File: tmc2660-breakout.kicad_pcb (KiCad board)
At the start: 2 copper layers, 26.9 x 31.1 mm, 21 parts, among them P1 SPI, P2 StepDir, P3 Motor, P4 VCC, P5 VMOT, U1 TMC2660

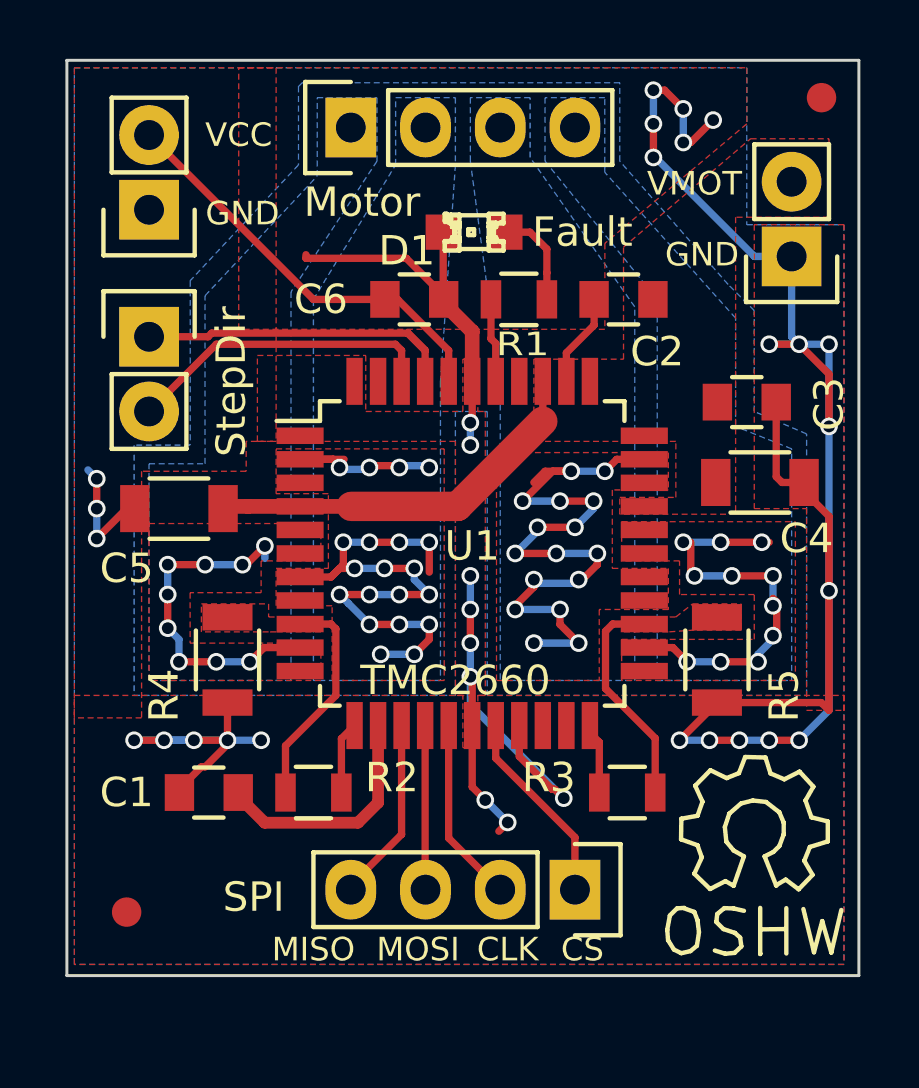
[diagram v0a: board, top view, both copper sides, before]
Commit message: o Add alternative footprint for shunt (2512 is more appropriate)
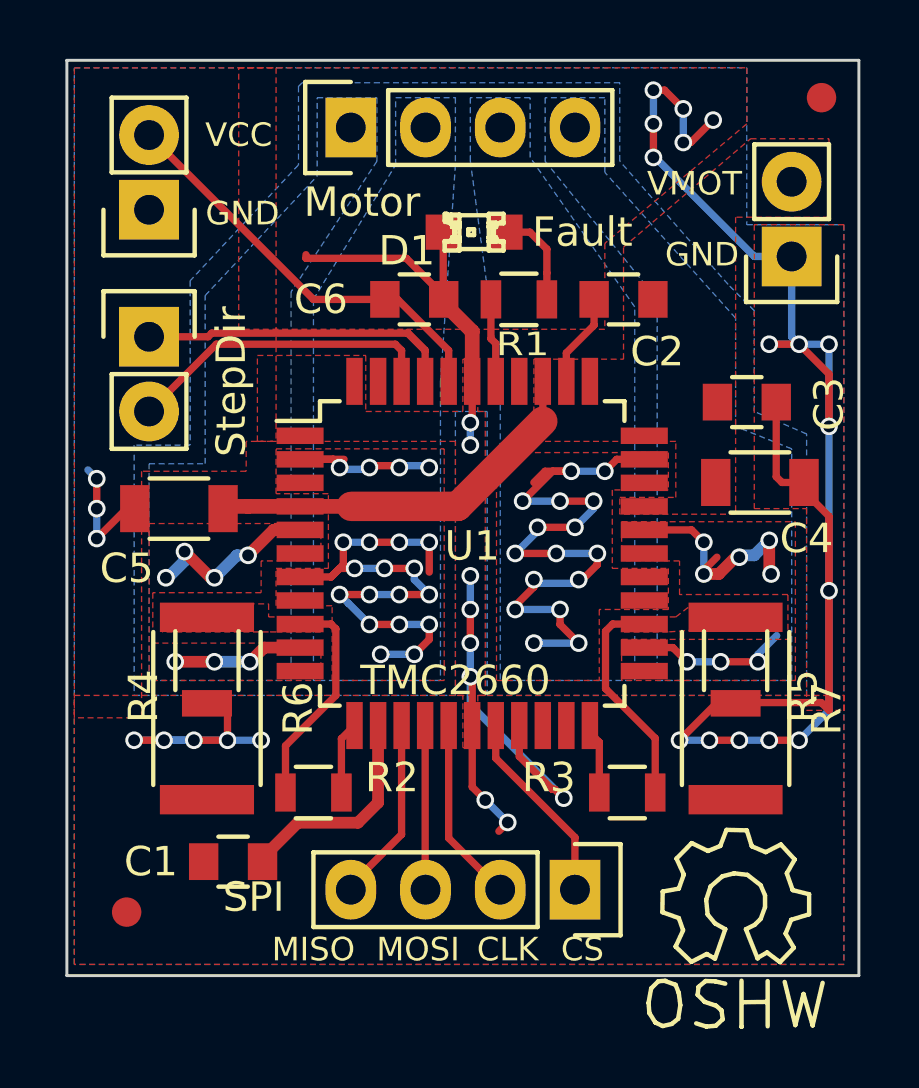
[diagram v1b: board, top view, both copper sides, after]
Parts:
- added R6: 0.075, Resistors_SMD:R_2512, F.Cu at (120.8, 59.6)
- added R7: 0.075, Resistors_SMD:R_2512, F.Cu at (138.8, 59.6)
- moved REF** 2.56 mm to (138.8, 66.2)
- moved C1 2.49 mm to (121.7, 64.8)
- moved R4 0.70 mm to (120.8, 58.0)
- moved R5 0.64 mm to (138.8, 58.0)
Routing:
- net GND: track 103.4 -> 101.0 mm
- net 1A2: track 11.9 -> 10.8 mm, vias 9 -> 7
- net Net-(C1-Pad1): track 8.15 -> 7.45 mm
- net 1B2: track 13.8 -> 13.2 mm, vias 11 -> 8

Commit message: o Widen the other 1206 pad to match the 2512 pad to avoid tombstoning
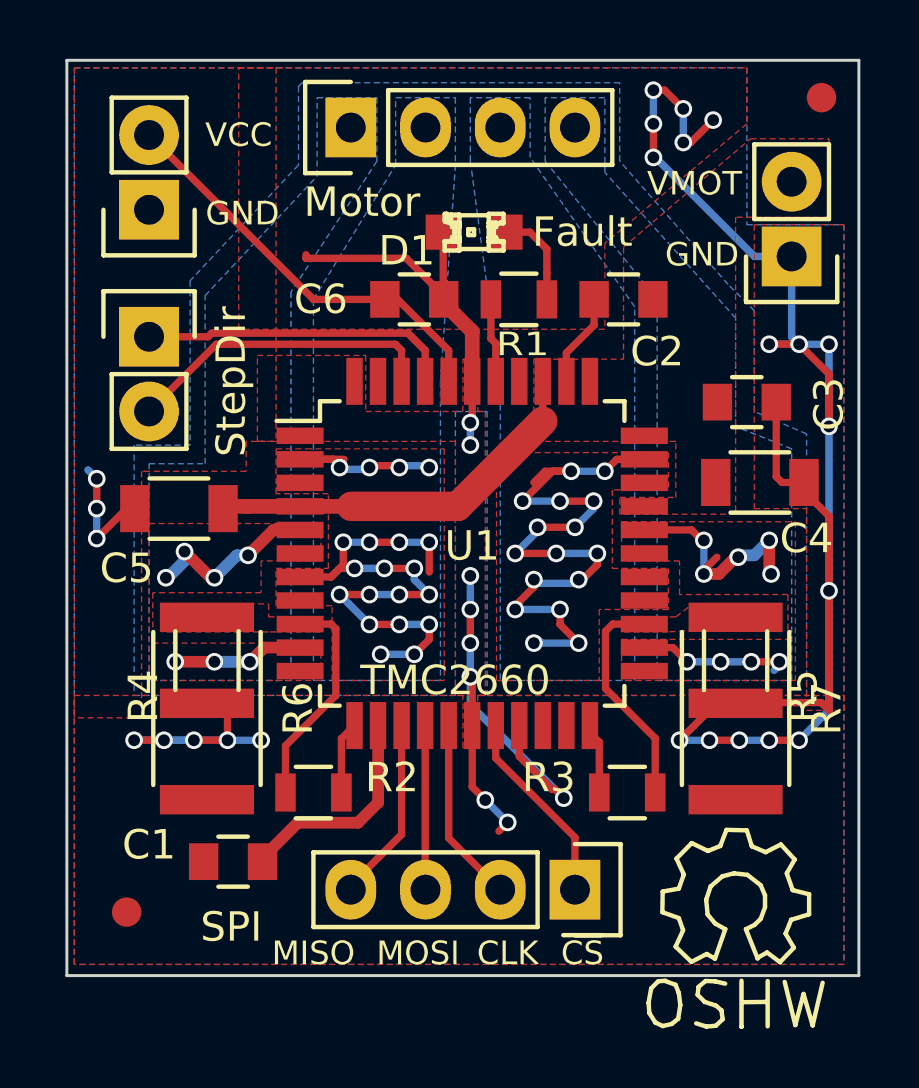
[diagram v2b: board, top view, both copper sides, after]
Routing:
- net 1B2: vias 8 -> 9
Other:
- board text added: "~CS"
- board text removed: "CS"
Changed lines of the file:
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@@
-(kicad_pcb (version 4) (host pcbnew "(2015-08-05 BZR 6054, Git 5c8efeb)-product")
+(kicad_pcb (version 4) (host pcbnew "(2016-01-05 BZR 6425, Git 89c183f)-product")
   (general
     (links 60)
@@
     (thickness 1.6)
     (drawings 13)
-    (tracks 312)
+    (tracks 314)
     (zones 0)
     (modules 23)
@@
   (layers
     (0 F.Cu signal)
-    (31 B.Cu signal hide)
+    (31 B.Cu signal)
     (32 B.Adhes user)
     (33 F.Adhes user)
@@
   )
   (setup
-    (last_trace_width 0.4)
+    (last_trace_width 0.25)
     (user_trace_width 0.4)
     (trace_clearance 0.127)
@@
     (mod_text_size 1 1)
     (mod_text_width 0.15)
-    (pad_size 1.5 1.5)
-    (pad_drill 0.6)
+    (pad_size 1 3.2)
+    (pad_drill 0)
     (pad_to_mask_clearance 0)
     (aux_axis_origin 0 0)
@@
     (pad 1 smd rect (at -1.45 0 270) (size 0.9 1.7) (layers F.Cu F.Paste F.Mask)
       (net 5 "Net-(R3-Pad1)"))
-    (pad 2 smd rect (at 1.45 0 270) (size 0.9 1.7) (layers F.Cu F.Paste F.Mask)
+    (pad 2 smd rect (at 1.45 0 270) (size 1 3.2) (layers F.Cu F.Paste F.Mask)
       (net 7 GND))
   )
@@
     (tags "capacitor 0805")
     (attr smd)
-    (fp_text reference C1 (at 2.794 0 180) (layer F.SilkS)
-      (effects (font (size 1 1) (thickness 0.15)))
-    )
-    (fp_text value 470n (at 1.016 -1.778 180) (layer F.Fab)
+    (fp_text reference C1 (at 2.8575 0.5715 180) (layer F.SilkS)
+      (effects (font (size 1 1) (thickness 0.15)))
+    )
+    (fp_text value 470n (at 3.8735 1.0795 180) (layer F.Fab)
       (effects (font (size 1 1) (thickness 0.15)))
     )
@@
       (effects (font (size 1 1) (thickness 0.15)))
     )
-    (fp_text value SPI (at 0.254 10.922 360) (layer F.SilkS)
+    (fp_text value SPI (at 1.27 11.684 360) (layer F.SilkS)
       (effects (font (size 1 1) (thickness 0.15)))
     )
@@
     (pad 1 smd rect (at -1.45 0 270) (size 0.9 1.7) (layers F.Cu F.Paste F.Mask)
       (net 3 "Net-(R2-Pad1)"))
-    (pad 2 smd rect (at 1.45 0 270) (size 0.9 1.7) (layers F.Cu F.Paste F.Mask)
+    (pad 2 smd rect (at 1.45 0 270) (size 1 3.2) (layers F.Cu F.Paste F.Mask)
       (net 7 GND))
   )
@@
     (effects (font (size 0.8 0.8) (thickness 0.15)))
   )
-  (gr_text "MOSI\n" (at 128.016 67.818) (layer F.SilkS)
-    (effects (font (size 0.8 0.8) (thickness 0.2)))
-  )
-  (gr_text "CLK\n" (at 131.064 67.818) (layer F.SilkS)
-    (effects (font (size 0.8 0.8) (thickness 0.2)))
-  )
-  (gr_text CS (at 133.604 67.818) (layer F.SilkS)
-    (effects (font (size 0.8 0.8) (thickness 0.2)))
-  )
-  (gr_text "MISO\n" (at 124.46 67.818) (layer F.SilkS)
-    (effects (font (size 0.8 0.8) (thickness 0.2)))
+  (gr_text "MOSI\n" (at 128.016 67.945) (layer F.SilkS)
+    (effects (font (size 0.8 0.8) (thickness 0.15)))
+  )
+  (gr_text "CLK\n" (at 131.064 67.945) (layer F.SilkS)
+    (effects (font (size 0.8 0.8) (thickness 0.15)))
+  )
+  (gr_text ~CS (at 133.604 67.945) (layer F.SilkS)
+    (effects (font (size 0.8 0.8) (thickness 0.15)))
+  )
+  (gr_text "MISO\n" (at 124.46 67.945) (layer F.SilkS)
+    (effects (font (size 0.8 0.8) (thickness 0.15)))
   )
   (gr_text %%gitversion%% (at 123.952 64.008 90) (layer B.SilkS)
@@
   (segment (start 134.772 51.156) (end 134.366 51.562) (width 0.25) (layer F.Cu) (net 19))
   (via (at 134.366 51.562) (size 0.6) (drill 0.4) (layers F.Cu B.Cu) (net 19))
+  (segment (start 140.2969 58.039) (end 140.2969 58.1533) (width 0.25) (layer B.Cu) (net 20))
+  (segment (start 140.2969 58.1533) (end 140.1191 58.3311) (width 0.25) (layer B.Cu) (net 20))
+  (segment (start 139.3444 58.039) (end 140.2969 58.039) (width 0.25) (layer F.Cu) (net 20))
+  (via (at 140.2969 58.039) (size 0.6) (drill 0.4) (layers F.Cu B.Cu) (net 20))
+  (segment (start 138.303 58.039) (end 139.3444 58.039) (width 0.25) (layer B.Cu) (net 20))
+  (via (at 139.3444 58.039) (size 0.6) (drill 0.4) (layers F.Cu B.Cu) (net 20))
   (segment (start 139.954 53.9115) (end 139.954 54.991) (width 0.4) (layer F.Cu) (net 20))
   (segment (start 139.954 54.991) (end 140.0175 55.0545) (width 0.4) (layer F.Cu) (net 20))
@@
   (segment (start 137.7315 55.0545) (end 138.2395 55.0545) (width 0.4) (layer F.Cu) (net 20))
   (segment (start 138.2395 55.0545) (end 138.8745 54.4195) (width 0.4) (layer F.Cu) (net 20))
-  (via (at 138.938 54.483) (size 0.6) (drill 0.4) (layers F.Cu B.Cu) (net 20))
+  (via (at 138.8999 54.483) (size 0.6) (drill 0.4) (layers F.Cu B.Cu) (net 20))
   (segment (start 137.6045 55.0545) (end 138.176 54.483) (width 0.25) (layer F.Cu) (net 20))
   (segment (start 137.7315 53.975) (end 137.7315 54.9275) (width 0.25) (layer B.Cu) (net 20))
@@
   (segment (start 135.7075 53.556) (end 137.3125 53.556) (width 0.25) (layer F.Cu) (net 20))
   (segment (start 137.3125 53.556) (end 137.7315 53.975) (width 0.25) (layer F.Cu) (net 20))
-  (via (at 137.7315 53.975) (size 0.6) (drill 0.4) (layers F.Cu B.Cu) (net 20))
-  (segment (start 139.573 58.039) (end 139.573 57.785) (width 0.25) (layer B.Cu) (net 20))
-  (segment (start 139.573 57.785) (end 140.208 57.15) (width 0.25) (layer B.Cu) (net 20))
-  (segment (start 138.303 58.039) (end 139.573 58.039) (width 0.25) (layer F.Cu) (net 20))
-  (via (at 139.573 58.039) (size 0.6) (drill 0.4) (layers F.Cu B.Cu) (net 20))
+  (via (at 137.7315 53.9115) (size 0.6) (drill 0.4) (layers F.Cu B.Cu) (net 20))
   (segment (start 137.16 58.039) (end 138.303 58.039) (width 0.25) (layer B.Cu) (net 20))
   (via (at 138.303 58.039) (size 0.6) (drill 0.4) (layers F.Cu B.Cu) (net 20))

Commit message: o Add optional filter caps for sense input. o Connect CLK input to GND to enable internal clock. o Fix typo in sense decoupling resistor (10k -> 10R)
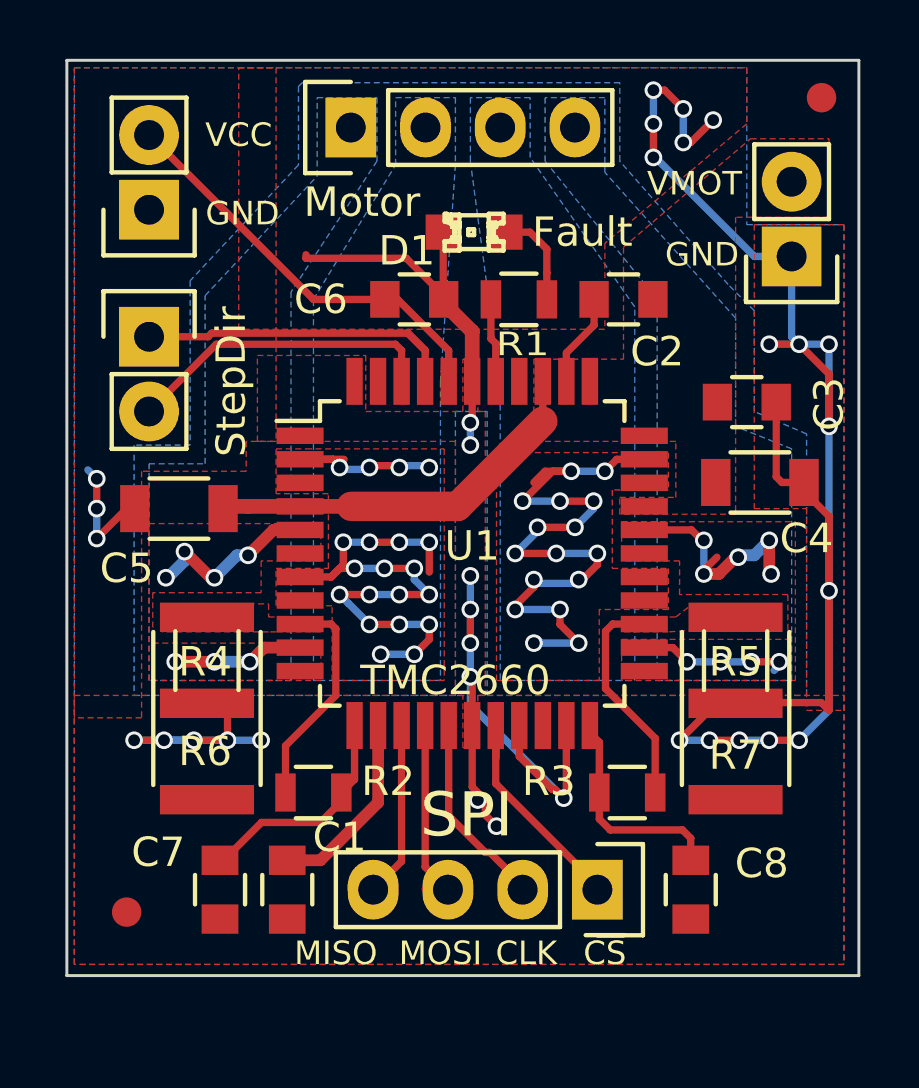
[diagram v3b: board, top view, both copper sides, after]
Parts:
- added C7: 10n, Capacitors_SMD:C_0805, F.Cu at (121.3, 65.8)
- added C8: 10n, Capacitors_SMD:C_0805, F.Cu at (137.3, 65.8)
- R2, R3: value 10k -> 10R
- REF**: moved to B.Cu
- moved REF** 23.6 mm to (128.5, 45.0), turned to 270 degrees
- moved C1 2.07 mm to (123.6, 65.8), turned to 270 degrees
- moved P1 0.76 mm to (134.1, 65.8)
- turned R2 to 180 degrees
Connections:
- net Net-(R3-Pad1) renamed /BRB
- R2 pad 1: Net-(R2-Pad1) -> Net-(C7-Pad2)
- R2 pad 2: Net-(R2-Pad2) -> /BRA
- R4 pad 1: Net-(R2-Pad1) -> /BRA
- R6 pad 1: Net-(R2-Pad1) -> /BRA
- U1 pad 12: Net-(R2-Pad2) -> Net-(C7-Pad2)
- U1 pad 21: (no net) -> GND
- U1 pad 9: Net-(R2-Pad1) -> /BRA
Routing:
- net /BRA: track 0.00 -> 8.42 mm
- net Net-(R2-Pad1): track 8.12 -> 0.00 mm
- net Net-(C7-Pad2): track 0.00 -> 7.97 mm
- net Net-(C8-Pad1): track 2.41 -> 7.74 mm
- net Net-(R2-Pad2): track 2.46 -> 0.00 mm
- net GND: track 101.0 -> 103.1 mm
- net Net-(P1-Pad1): track 6.70 -> 8.12 mm
- net Net-(C1-Pad1): track 7.45 -> 6.52 mm
- added copper zone on F.Cu, net /BRA
- removed copper zone on F.Cu, net Net-(R2-Pad1)
